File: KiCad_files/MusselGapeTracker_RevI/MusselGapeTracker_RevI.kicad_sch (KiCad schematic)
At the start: 83 parts, among them J1 AVR_SPI_PRG_6PTH, U1 ATMEGA328P, U2 DS3231M+TRL, U3 DS3231MZ

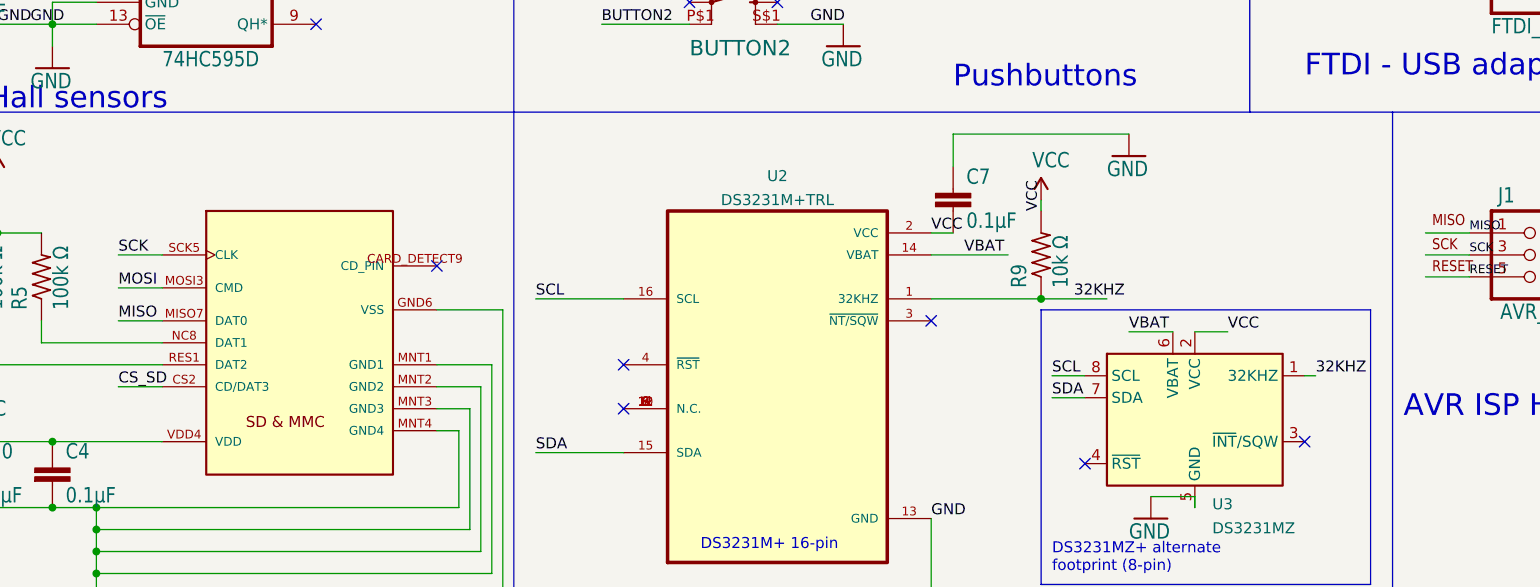
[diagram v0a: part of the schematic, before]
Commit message: Moved changes to Rev I and fixed DRC errors
Made new copy of KiCad project in Rev I and fixed some electric rules checker errors and warnings and some design rules checker errors and warnings
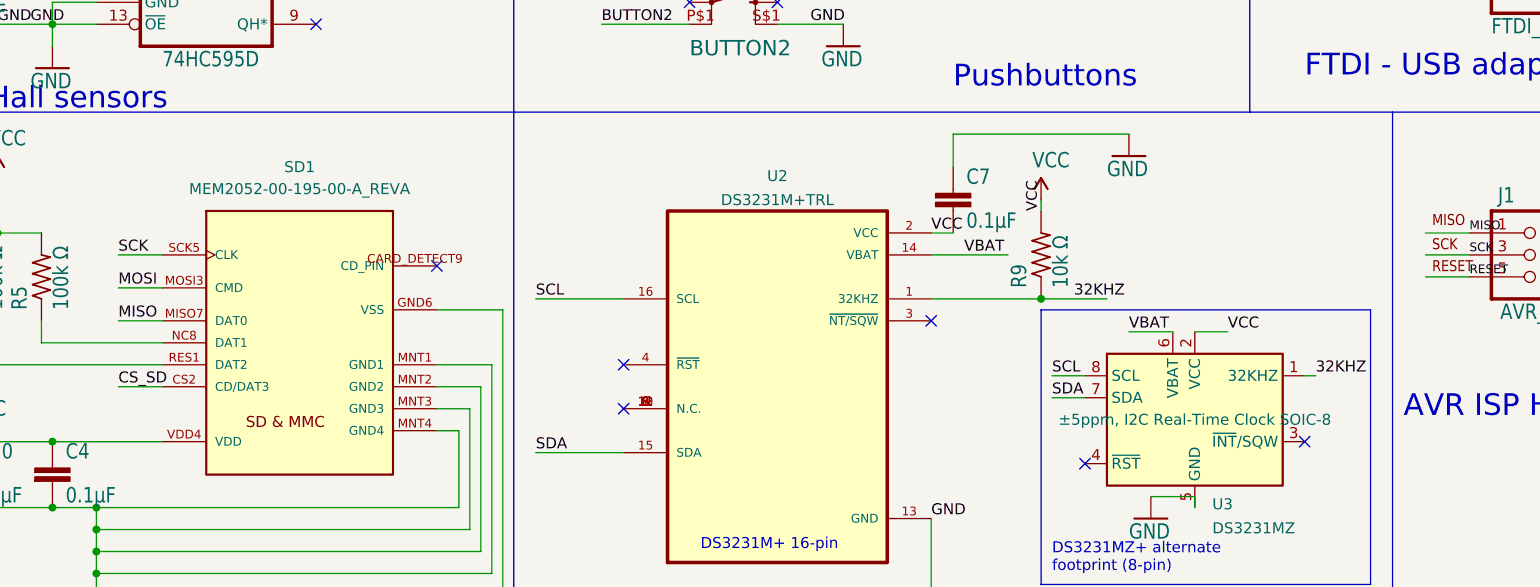
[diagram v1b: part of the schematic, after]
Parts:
- removed SD1: GCT_MEM2052-00-195-00-A_REVA, MusselGapeTracker_RevH:GCT_MEM2052-00-195-00-A_REVA, symbol MusselGapeTracker_RevH-SlaterSymbols:MEM2052-00-195-00-A_REVA
- added SD1: MEM2052-00-195-00-A_REVA, MusselGapeTracker_RevI:GCT_MEM2052-00-195-00-A_REVA, symbol MusselGapeTracker_RevI:MEM2052-00-195-00-A_REVA
- BJT0: footprint MusselGapeTracker_RevE:SOT23 -> MusselGapeTracker_RevI:SOT23; symbol MusselGapeTracker_RevE-eagle-import:KSC1623_BJT_TRANSISTOR -> MusselGapeTracker_RevI:KSC1623_BJT_TRANSISTOR
- BUTTON1, BUTTON2: footprint MusselGapeTracker_RevE:PUSHBUTTON_DPST_SMD -> MusselGapeTracker_RevI:PUSHBUTTON_DPST_SMD; symbol MusselGapeTracker_RevE-eagle-import:PUSHBUTTON_DPST_SMDSTANDARD -> MusselGapeTracker_RevI:PUSHBUTTON_DPST_SMDSTANDARD
- C1, C2: footprint MusselGapeTracker_RevE:PANASONIC_B -> MusselGapeTracker_RevI:PANASONIC_B; symbol MusselGapeTracker_RevE-eagle-import:CPOL-USB -> MusselGapeTracker_RevI:CPOL-USB
- C10, C23, C3, C4, C5, C6, C7, C8, C9: symbol MusselGapeTracker_RevE-eagle-import:CAP0603 -> MusselGapeTracker_RevI:CAP0603
- CR1220_BATTERY0: footprint MusselGapeTracker_RevE:CR1220_BATTERY_HOLDER_SMD -> MusselGapeTracker_RevI:CR1220_BATTERY_HOLDER_SMD; symbol MusselGapeTracker_RevE-eagle-import:CR1220_BATTERY_HOLDERSMD -> MusselGapeTracker_RevI:CR1220_BATTERY_HOLDERSMD
- GND0, PB7, U$10, U$11, U$17, U$3, U$4, U$6, U$7, U$8, U$9: footprint MusselGapeTracker_RevE:1X01_SMALL -> MusselGapeTracker_RevI:1X01_SMALL; symbol MusselGapeTracker_RevE-eagle-import:PINHD-1X1SMALL -> MusselGapeTracker_RevI:PINHD-1X1SMALL
- GROUND_CON0: footprint MusselGapeTracker_RevE:SJ_2S-TRACE -> MusselGapeTracker_RevI:SJ_2S-TRACE; symbol MusselGapeTracker_RevE-eagle-import:SOLDER_JUMPER_TRACESTANDARD -> MusselGapeTracker_RevI:SOLDER_JUMPER_TRACESTANDARD
- HALL0, HALL1, HALL10, HALL11, HALL12, HALL13, HALL14, HALL15, HALL2, HALL3, HALL4, HALL5, HALL6, HALL7, HALL8, HALL9: footprint MusselGapeTracker_RevE:JST-PH-4-THM -> MusselGapeTracker_RevI:JST-PH-4-THM; symbol MusselGapeTracker_RevE-eagle-import:JST-4PINTH_STRAIGHT -> MusselGapeTracker_RevI:JST-4PINTH_STRAIGHT
- INDUCTOR0: footprint MusselGapeTracker_RevE:I_0805 -> MusselGapeTracker_RevI:I_0805; symbol MusselGapeTracker_RevE-eagle-import:INDUCTOR0805_TY -> MusselGapeTracker_RevI:INDUCTOR0805_TY
- J1: footprint MusselGapeTracker_RevE:2X3 -> MusselGapeTracker_RevI:2X3; symbol MusselGapeTracker_RevE-eagle-import:AVR_SPI_PRG_6PTH -> MusselGapeTracker_RevI:AVR_SPI_PRG_6PTH
- JP1: footprint MusselGapeTracker_RevE:1X06-RIGHT_ANGLE -> MusselGapeTracker_RevI:1X06-RIGHT_ANGLE; symbol MusselGapeTracker_RevE-eagle-import:PINHD-1X6RA -> MusselGapeTracker_RevI:PINHD-1X6RA
- LED1, LED2: footprint MusselGapeTracker_RevE:CHIPLED_0805 -> MusselGapeTracker_RevI:CHIPLED_0805; symbol MusselGapeTracker_RevE-eagle-import:LED0805 -> MusselGapeTracker_RevI:LED0805
- MCP1700T-3302: footprint MusselGapeTracker_RevE:SOT95P237X112-3N -> MusselGapeTracker_RevI:SOT95P237X112-3N; symbol MusselGapeTracker_RevE-eagle-import:MCP1700T-3302E/TT -> MusselGapeTracker_RevI:MCP1700T-3302E/TT
- MOLEX_KK0: footprint MusselGapeTracker_RevE:22-23-2021 -> MusselGapeTracker_RevI:22-23-2021; symbol MusselGapeTracker_RevE-eagle-import:22-23-2021 -> MusselGapeTracker_RevI:22-23-2021
- OLED0: footprint MusselGapeTracker_RevE:1X04_LOCK -> MusselGapeTracker_RevI:1X04_LOCK; symbol MusselGapeTracker_RevE-eagle-import:PINHD-1X4LOCK -> MusselGapeTracker_RevI:PINHD-1X4LOCK
- PFET-0: footprint MusselGapeTracker_RevH:SOT23-3 -> MusselGapeTracker_RevI:SOT23-3; symbol MusselGapeTracker_RevE-eagle-import:MOSFET-PCHANNELSSM3J328R -> MusselGapeTracker_RevI:MOSFET-PCHANNELSSM3J328R
- R1, R14, R15, R2, R28, R29, R3, R30, R31, R32, R33, R4, R5, R6, R7, R8, R9: symbol MusselGapeTracker_RevE-eagle-import:RESISTOR_SMDR0603 -> MusselGapeTracker_RevI:RESISTOR_SMDR0603
- RESET0: footprint MusselGapeTracker_RevE:PUSHBUTTON_SPST_PTS525_SERIES -> MusselGapeTracker_RevI:PUSHBUTTON_SPST_PTS525_SERIES; symbol MusselGapeTracker_RevE-eagle-import:PUSHBUTTON_DPST_SMDSMALL -> MusselGapeTracker_RevI:PUSHBUTTON_DPST_SMDSMALL
- SHIFT_0, SHIFT_1: footprint MusselGapeTracker_RevE:SO16 -> MusselGapeTracker_RevI:SO16; symbol MusselGapeTracker_RevE-eagle-import:74HC595D -> MusselGapeTracker_RevI:74HC595D
- STANDOFF1, STANDOFF2, STANDOFF3: footprint MusselGapeTracker_RevE:STAND-OFF -> MusselGapeTracker_RevI:STAND-OFF; symbol MusselGapeTracker_RevE-eagle-import:STAND-OFF4-40 -> MusselGapeTracker_RevI:STAND-OFF4-40
- STANDOFF4_M2, STANDOFF5_M2: footprint MusselGapeTracker_RevE:STAND-OFF_M2 -> MusselGapeTracker_RevI:STAND-OFF_M2; symbol MusselGapeTracker_RevE-eagle-import:STAND-OFFM2 -> MusselGapeTracker_RevI:STAND-OFFM2
- U$2: symbol MusselGapeTracker_RevE-eagle-import:74HC4067SM96 -> MusselGapeTracker_RevI:74HC4067SM96
- U1: footprint MusselGapeTracker_RevE:TQFP32-08 -> MusselGapeTracker_RevI:TQFP32-08; symbol MusselGapeTracker_RevE-eagle-import:ATMEGA328_SMT -> MusselGapeTracker_RevI:ATMEGA328_SMT
- UNK2,1MM_JACK0: footprint MusselGapeTracker_RevE:POWER_JACK_DC_2,1MM -> MusselGapeTracker_RevI:POWER_JACK_DC_2,1MM; symbol MusselGapeTracker_RevE-eagle-import:POWER_JACK_2,1MM -> MusselGapeTracker_RevI:POWER_JACK_2,1MM
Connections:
- net CS_SD: now also SD1.CS2 (CD/DAT3)
- net GND: now also SD1.GND6 (VSS), SD1.MNT1 (GND1), SD1.MNT2 (GND2), SD1.MNT3 (GND3), SD1.MNT4 (GND4)
- net MISO: now also SD1.MISO7 (DAT0)
- net MOSI: now also SD1.MOSI3 (CMD)
- net SCK: now also SD1.SCK5 (CLK)
- net VCC: now also SD1.VDD4 (VDD)
- net at R4.1: now also SD1.RES1 (DAT2)
- net at R5.1: now also SD1.NC8 (DAT1)

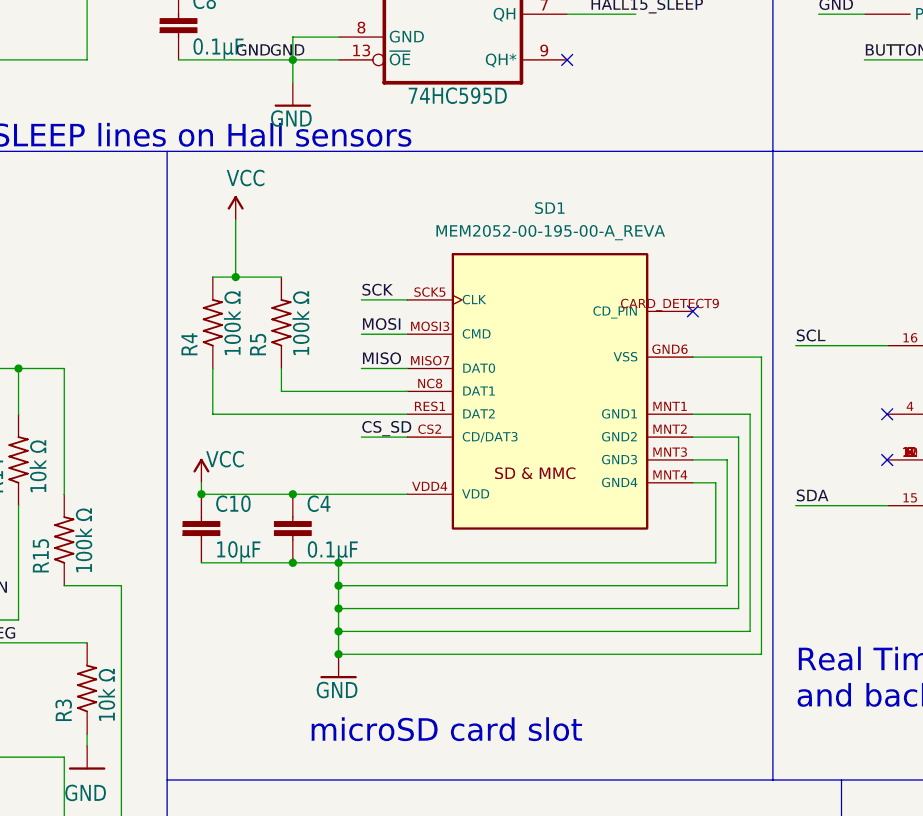
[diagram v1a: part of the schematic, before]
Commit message: Updated KiCad and Parts list for new SD Card Slot
Updated KiCad schematic, PCB, and parts list for new SD card slot Molex 5033981892
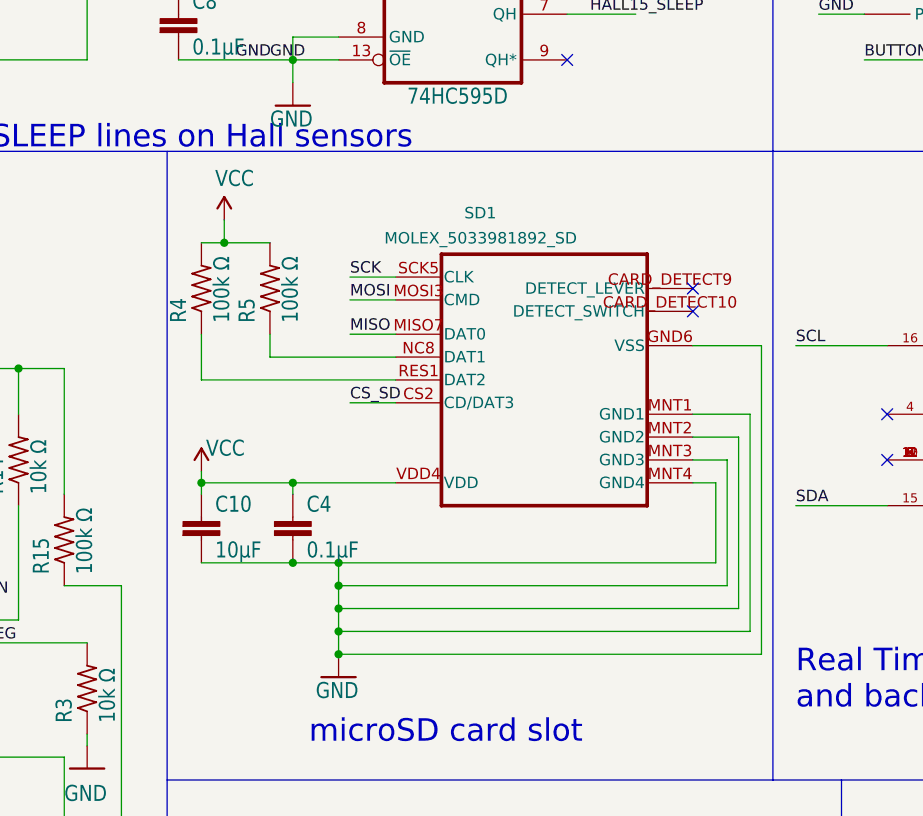
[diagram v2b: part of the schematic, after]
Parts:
- SD1: value MEM2052-00-195-00-A_REVA -> MOLEX_5033981892_SD; footprint MusselGapeTracker_RevI:GCT_MEM2052-00-195-00-A_REVA -> MusselGapeTracker_RevI:CONN_503398-1892_MOL; symbol MusselGapeTracker_RevI:MEM2052-00-195-00-A_REVA -> MusselGapeTracker_RevI:MOLEX_5033981892
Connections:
- no-connect marks 14 -> 15
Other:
- moved on the sheet: R4, R5

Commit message: Fixed SD card mount traces
Ran SD card traces on bottom instead of top to avoid sd mount prohibition area
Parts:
- R1, R2: value 100 Ω -> 100
- R14, R3, R6, R9: value 10k Ω -> 10k
- R15, R4, R5: value 100k Ω -> 100k
- R28: value 10kΩ -> 10k
- U4: renamed from U$2; value 74HC4067SM96 -> CD74HC4067PWR
- renumbered MCP1700T-3302 to MCP1700T3302
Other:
- moved on the sheet: BJT0, BUTTON1, BUTTON2, C1, C10, C2, C23, C3, C4, C5, C6, C7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
